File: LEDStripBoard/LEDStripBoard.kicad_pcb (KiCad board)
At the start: 2 copper layers, 50 x 44 mm, 32 parts, among them J1 Conn_01x09, J2 Barrel_Jack, J3 Conn_01x04, U1 STCS2, U1 TP TestPoint, U2 STCS2, U2 TP TestPoint, U3 STCS2, U3 TP TestPoint

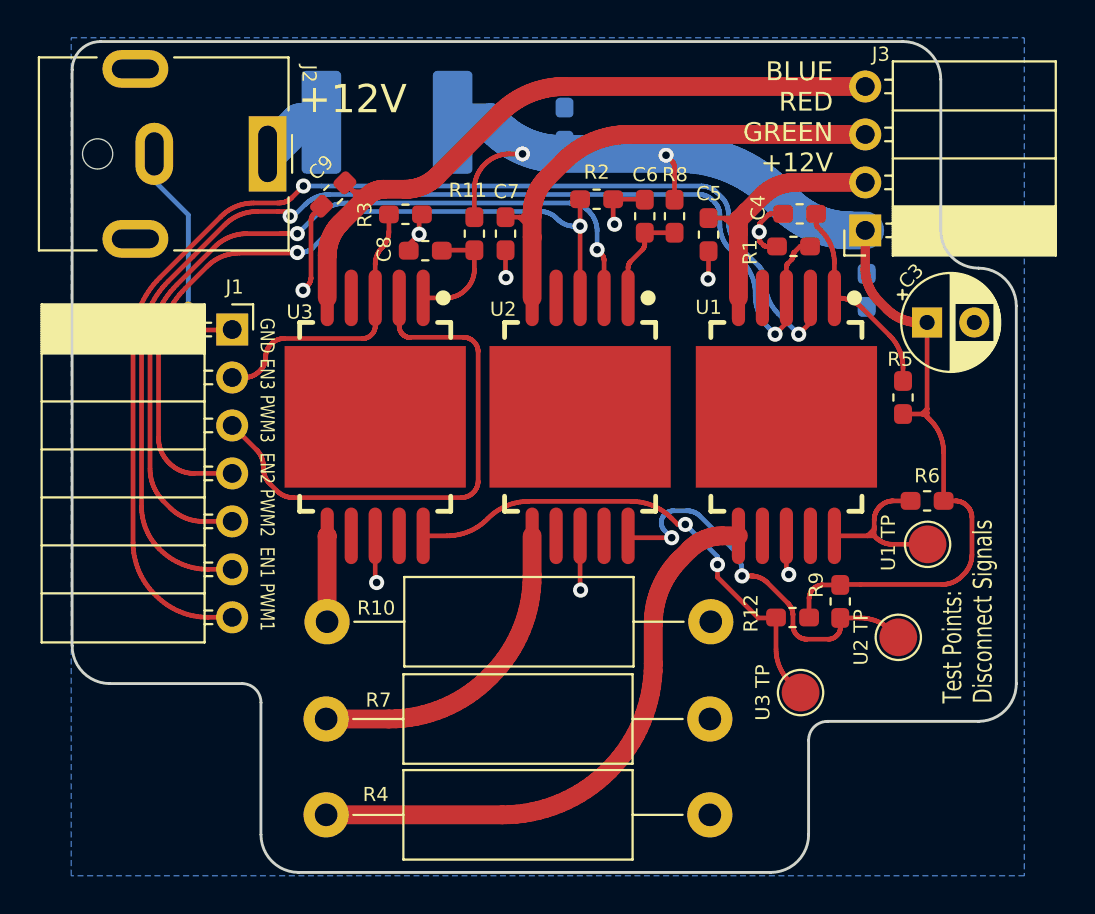
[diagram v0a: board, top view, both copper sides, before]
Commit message: Add vcc Diode
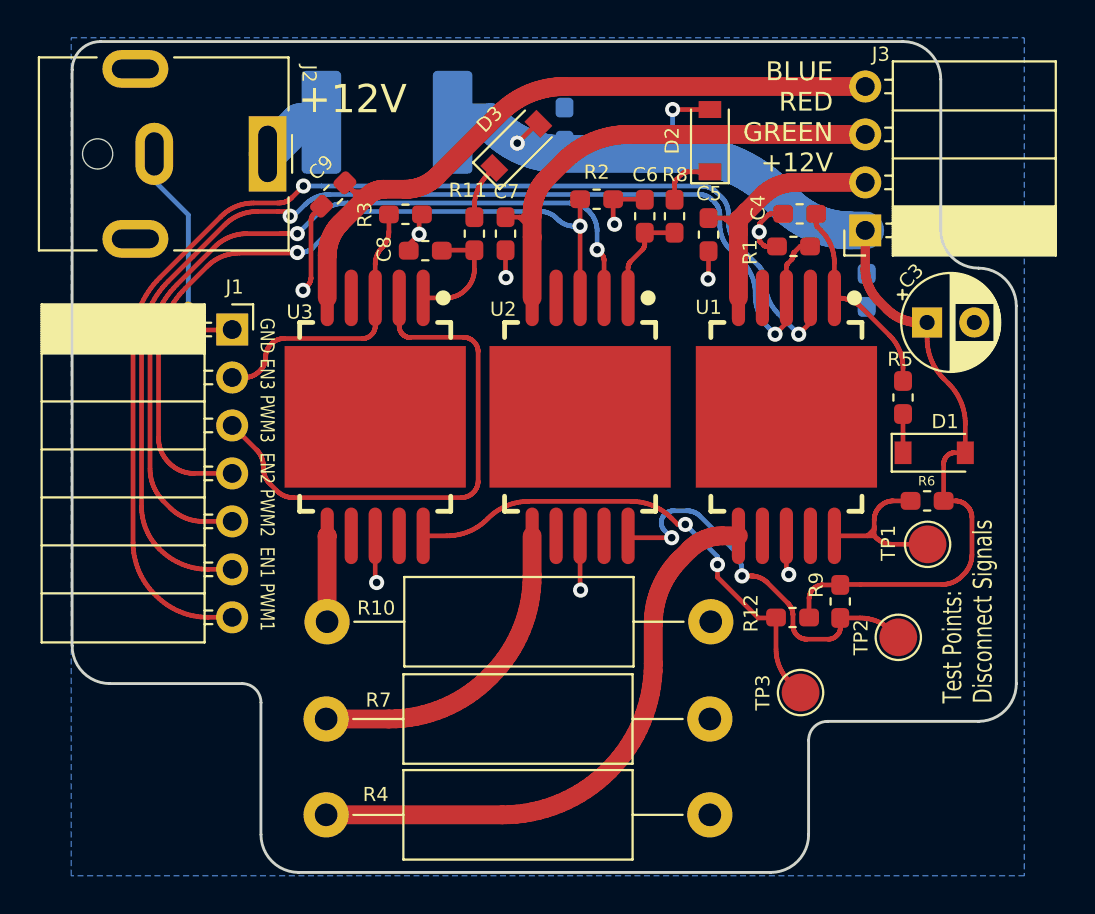
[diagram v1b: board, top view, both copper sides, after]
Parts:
- added D1: BAT46, Diode_SMD:D_SOD-123, F.Cu at (145.7, 71.8)
- added D2: BAT46, Diode_SMD:D_SOD-123, F.Cu at (133.8, 55.2)
- added D3: BAT46, Diode_SMD:D_SOD-123, F.Cu at (123.5, 55.5)
- J1: value Conn_01x09 -> Conn_01x07
- TP1: renamed from U1 TP
- TP2: renamed from U2 TP
- TP3: renamed from U3 TP
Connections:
- R11 pad 1: +12V -> Net-(D3-Pad1)
- R5 pad 1: +12V -> Net-(D1-Pad1)
- R8 pad 1: +12V -> Net-(D2-Pad1)
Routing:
- net Net-(D2-Pad1): track 0.00 -> 3.02 mm
- net Net-(D3-Pad1): track 0.00 -> 2.94 mm
- net +12V: track 66.8 -> 69.6 mm
- net Net-(D1-Pad1): track 0.00 -> 2.05 mm
